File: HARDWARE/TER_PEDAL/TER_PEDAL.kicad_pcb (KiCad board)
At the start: 4 copper layers, 78.6 x 34.5 mm, 58 parts, among them J1 DEBUG, J2 APPS_1, J3 RJ45_Shielded, J4 APPS_2, J5 BPPS_1, J6 SteerSensor, SW1 RST, U1 STM32F103C8Tx, U2 TSR_1-2450, U3 LM1117MP-3.3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

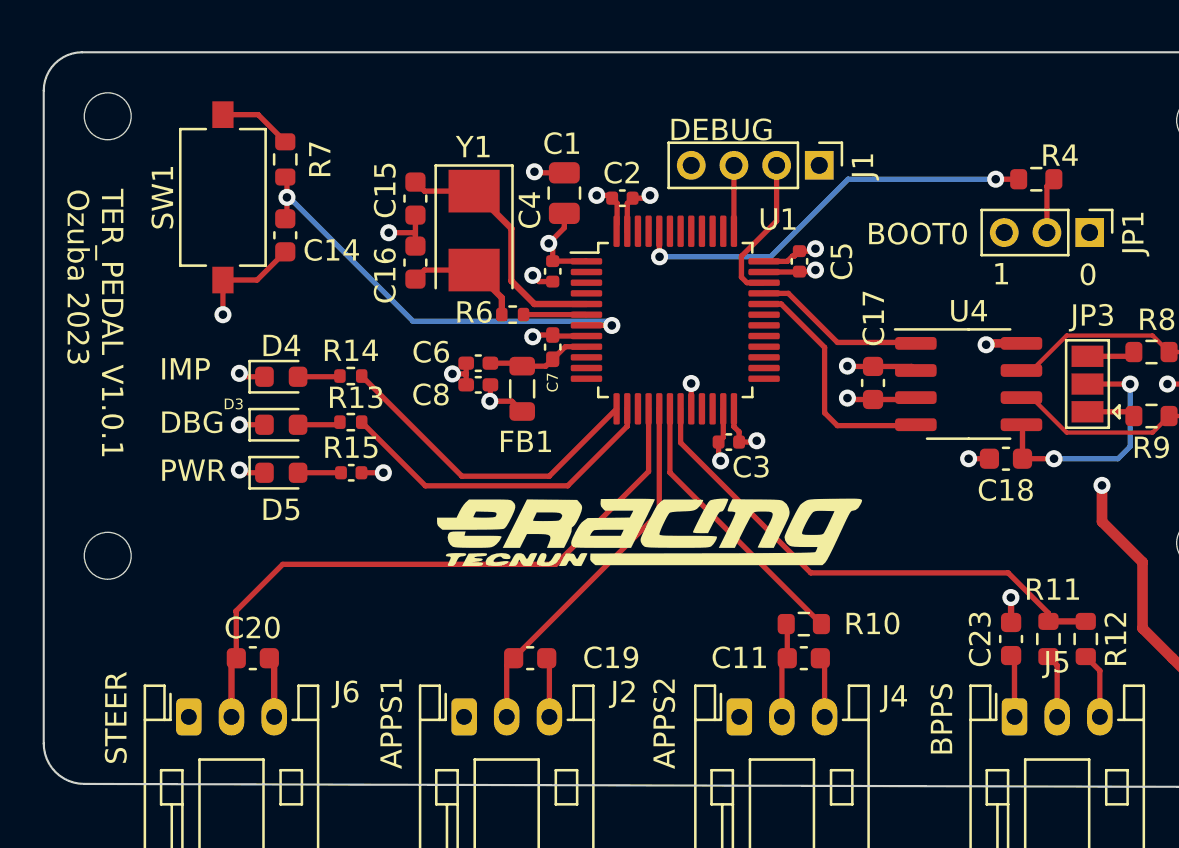
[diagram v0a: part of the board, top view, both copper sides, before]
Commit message: Added pull down resistors for adc to prevent floating value when disconnected signals, added LABELS lots of labels
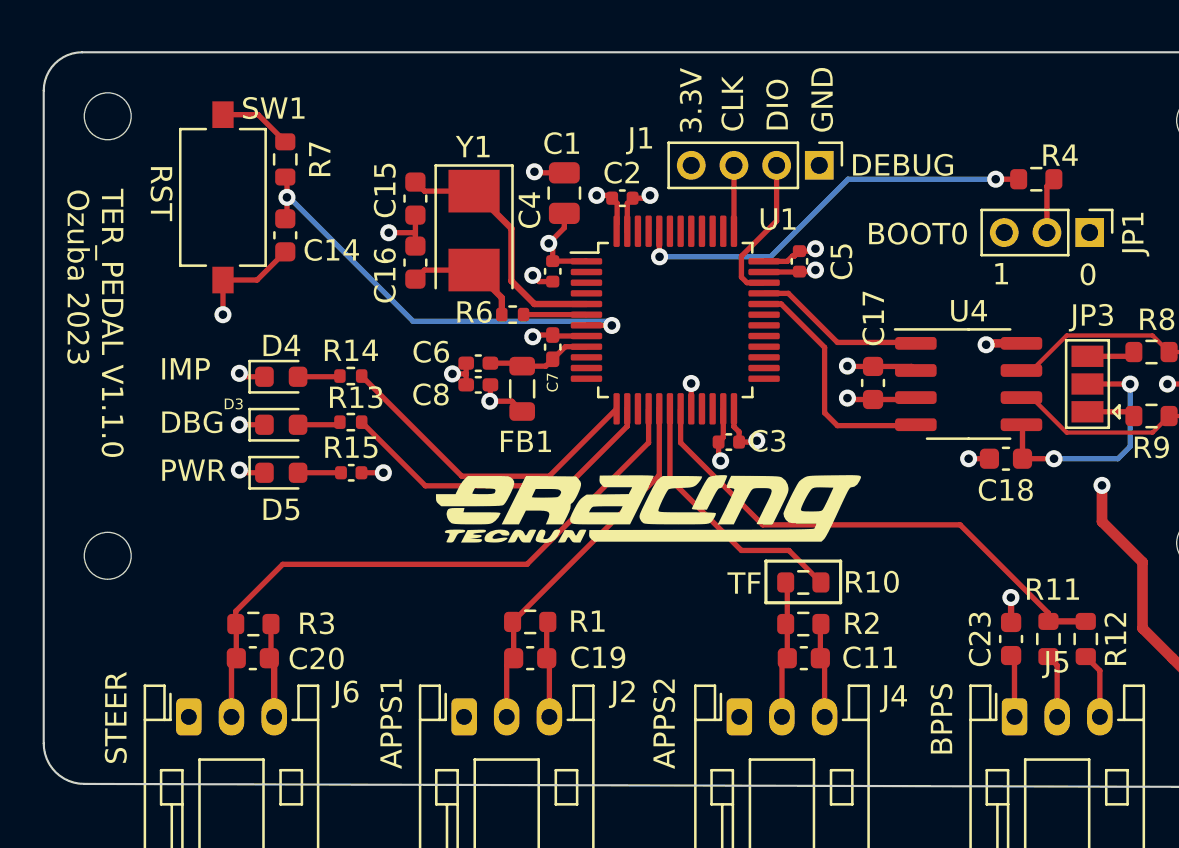
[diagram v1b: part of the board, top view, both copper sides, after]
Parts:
- added R1: 10k, Resistor_SMD:R_0603_1608Metric, F.Cu at (134.2, 102.9)
- added R2: 10k, Resistor_SMD:R_0603_1608Metric, F.Cu at (147.0, 103.0)
- added R3: 10k, Resistor_SMD:R_0603_1608Metric, F.Cu at (121.2, 103.0)
- moved R10 1.95 mm to (147.0, 101.0)
- moved G*** 1.10 mm to (139.8, 97.6)
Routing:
- net GND: track 57.0 -> 61.9 mm
- net /SENSORS/SENS_2: track 4.47 -> 6.43 mm
- net /MICRO/STEER_ADC: track 30.1 -> 29.3 mm
- net /MICRO/APPS_2_ADC: track 13.0 -> 12.4 mm
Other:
- board text added: "3.3V"
- board text added: "CLK"
- board text added: "DIO"
- board text added: "GND"
- board text added: "RST"
- board text added: "TER_PEDAL V1.1.0 Ozuba 2023"
- board text added: "TF"
- board text removed: "TER_PEDAL V1.0.1 Ozuba 2023"

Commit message: condensador señal brake
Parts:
- removed C23: 10u, Capacitor_SMD:C_0603_1608Metric
- added C21: 390u, Capacitor_SMD:C_0603_1608Metric, F.Cu at (157.1, 103.9)
- moved R11 0.43 mm to (158.9, 103.9)
- moved R12 0.43 mm to (160.6, 103.9)
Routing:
- net +5V: track 6.84 -> 3.90 mm

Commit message: Hecho layout
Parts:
- removed C17: 100n, Capacitor_SMD:C_0603_1608Metric
- removed C18: 4.7n, Capacitor_SMD:C_0603_1608Metric
- removed J1: DEBUG, Connector_PinHeader_2.00mm:PinHeader_1x04_P2.00mm_Vertical
- removed JP3: TermEnable, Jumper:SolderJumper-3_P1.3mm_Open_Pad1.0x1.5mm
- added C31: 100nF, Capacitor_SMD:C_0603_1608Metric, F.Cu at (148.4, 91.7)
- added C32: 4.7nF, Capacitor_SMD:C_0603_1608Metric, F.Cu at (154.6, 95.2)
- added FL2: ACT45B-510-2P-TL003, ACT45B-510-2P-TL003:FIL_ACT45B-510-2P-TL003, F.Cu at (165.0, 91.9)
- added J7: DEBUG, Connector_PinHeader_1.27mm:PinHeader_2x05_P1.27mm_Vertical, F.Cu at (147.4, 78.3)
- added JP2: SolderJumper_3_Open, Jumper:SolderJumper-3_P1.3mm_Open_Pad1.0x1.5mm, B.Cu at (167.9, 92.1)
- added R16: 100k, Resistor_SMD:R_0603_1608Metric, F.Cu at (149.6, 78.9)
- added R32: 50R, Resistor_SMD:R_0805_2012Metric, F.Cu at (169.6, 94.3)
- added R5: 100k, Resistor_SMD:R_0603_1608Metric, F.Cu at (140.2, 79.0)
- R8: value 50R -> 100k
- R9: footprint Resistor_SMD:R_0603_1608Metric -> Resistor_SMD:R_0805_2012Metric
- moved R8 21.5 mm to (143.4, 82.0)
- moved R9 7.31 mm to (169.7, 89.7), turned to 90 degrees
- moved D2 7.27 mm to (159.6, 91.8), turned to 180 degrees
- moved U4 1.90 mm to (152.9, 91.7)
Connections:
- D2 pad 1: /CAN/CAN+ -> Net-(U4-CANL)
- D2 pad 2: /CAN/CAN- -> Net-(U4-CANH)
- R8 pad 1: /CAN/CAN+ -> /MICRO/SWCLK
- R8 pad 2: Net-(JP3-B) -> GND
- R9 pad 1: Net-(JP3-A) -> /CAN/CAN+
- R9 pad 2: /CAN/CAN- -> Net-(JP2-A)
- U4 pad 6: /CAN/CAN- -> Net-(U4-CANL)
- U4 pad 7: /CAN/CAN+ -> Net-(U4-CANH)
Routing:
- net /MICRO/NRST: track 20.9 -> 34.1 mm
- net /CAN/CAN+: track 19.4 -> 8.38 mm
- net /CAN/CAN-: track 21.1 -> 10.2 mm
- net Net-(U4-CANL): track 0.00 -> 8.20 mm
- net Net-(U4-CANH): track 0.00 -> 8.02 mm
- net /MICRO/SWDIO: track 7.09 -> 12.0 mm
- net /MICRO/SWCLK: track 3.09 -> 7.98 mm
- net Net-(JP2-A): track 0.00 -> 4.46 mm, vias 0 -> 1
- net Net-(JP2-B): track 0.00 -> 4.00 mm, vias 0 -> 1
- net +3.3V: track 41.8 -> 45.8 mm, vias 8 -> 9
- net /CAN/VREF: track 12.1 -> 15.7 mm, vias 2 -> 1
- net Net-(JP3-B): track 2.26 -> 0.00 mm
- net Net-(JP3-A): track 2.26 -> 0.00 mm
- net /CAN/CAN_TX: track 8.08 -> 6.22 mm
- net GND: track 61.5 -> 62.8 mm
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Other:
- board text removed: "3.3V"
- board text removed: "CLK"
- board text removed: "DIO"
- board text removed: "GND"

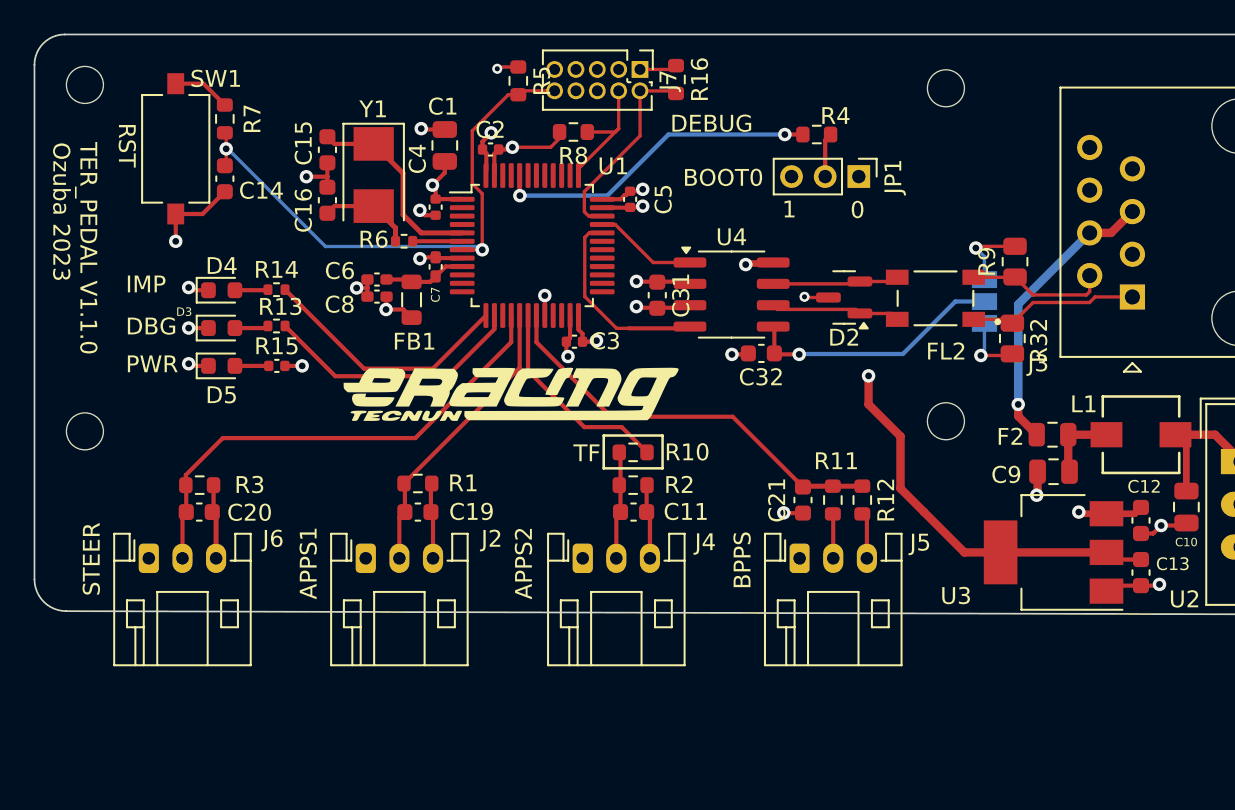
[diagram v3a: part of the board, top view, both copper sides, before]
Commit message: Added voltage followers to sensing, improved can circuitri, improved layout, waiting for routing
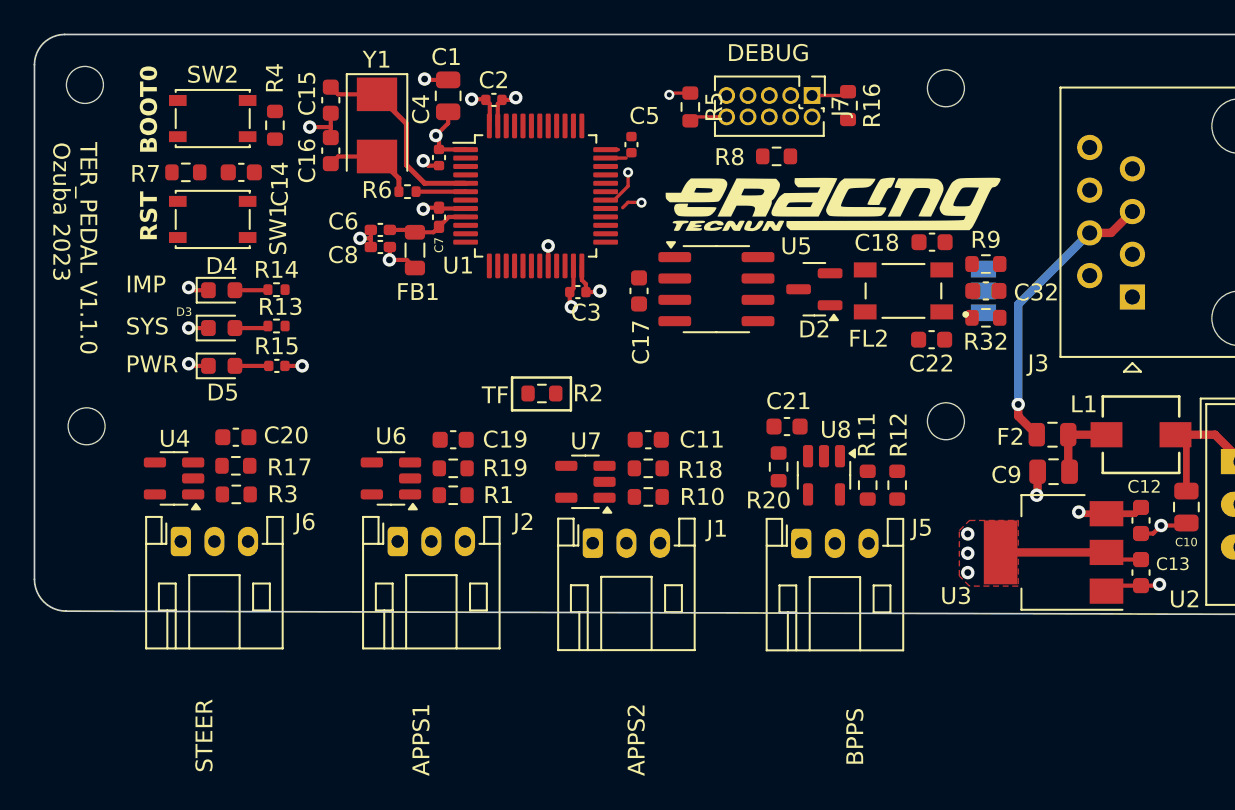
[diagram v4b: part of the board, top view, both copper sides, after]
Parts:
- removed C31: 100nF, Capacitor_SMD:C_0603_1608Metric
- removed J4: APPS_2, Connector_JST:JST_PH_S3B-PH-K_1x03_P2.00mm_Horizontal
- removed JP1: BOOT0, Connector_PinHeader_2.00mm:PinHeader_1x03_P2.00mm_Vertical
- added C17: 100n, Capacitor_SMD:C_0603_1608Metric, F.Cu at (147.3, 91.5)
- added C18: 10p, Capacitor_SMD:C_0603_1608Metric, F.Cu at (164.8, 88.5)
- added C22: 10p, Capacitor_SMD:C_0603_1608Metric, F.Cu at (164.8, 94.3)
- added J1: APPS_2, Connector_JST:JST_PH_S3B-PH-K_1x03_P2.00mm_Horizontal, F.Cu at (144.6, 106.5)
- added R17: 100, Resistor_SMD:R_0603_1608Metric, F.Cu at (123.4, 101.8)
- added R18: 100, Resistor_SMD:R_0603_1608Metric, F.Cu at (147.9, 102.0)
- added R19: 100, Resistor_SMD:R_0603_1608Metric, F.Cu at (136.3, 102.0)
- added R20: 100, Resistor_SMD:R_0603_1608Metric, F.Cu at (155.7, 101.9)
- added SW2: BOOT0, Button_Switch_SMD:SW_SPST_PTS810, F.Cu at (122.0, 81.2)
- added U5: TCAN332, Package_SO:SOIC-8_3.9x4.9mm_P1.27mm, F.Cu at (151.9, 91.3)
- added U6: LM321, Package_TO_SOT_SMD:SOT-23-5, F.Cu at (132.6, 102.6)
- added U7: LM321, Package_TO_SOT_SMD:SOT-23-5, F.Cu at (144.2, 102.8)
- added U8: LM321, Package_TO_SOT_SMD:SOT-23-5, F.Cu at (158.3, 102.4)
- C11, C19, C20: value 10u -> 160n
- C21: value 390u -> 160n
- D3: value LED -> SYS
- D4: value LED -> IMP
- D5: value LED -> PWR
- R1, R3: value 10k -> 100k
- R10: value 2k -> 100k
- R2: value 10k -> 0R
- R32, R9: value 50R -> 120R; footprint Resistor_SMD:R_0805_2012Metric -> Resistor_SMD:R_0603_1608Metric
- SW1: footprint Button_Switch_SMD:SW_Tactile_SPST_NO_Straight_CK_PTS636Sx25SMTRLFS -> Button_Switch_SMD:SW_SPST_PTS810
- U4: value SN65HVD230 -> LM321; footprint Package_SO:SOIC-8_3.9x4.9mm_P1.27mm -> Package_TO_SOT_SMD:SOT-23-5
- moved U4 34.9 mm to (119.7, 102.6), turned to 180 degrees
- moved R4 32.2 mm to (125.7, 81.6), turned to 90 degrees
- moved G*** 22.2 mm to (158.9, 86.3)
- moved C32 13.9 mm to (168.0, 91.5)
- moved R8 12.2 mm to (155.5, 83.5)
- moved R5 10.3 mm to (150.4, 80.5)
- moved R16 10.3 mm to (159.8, 80.4)
- moved J7 10.3 mm to (157.6, 79.8)
- moved R2 7.69 mm to (141.6, 97.5)
- moved C20 4.95 mm to (123.4, 100.2), turned to 180 degrees
- moved C19 4.79 mm to (136.3, 100.3), turned to 180 degrees
- moved SW1 4.74 mm to (122.0, 87.2), turned to 180 degrees
- moved C21 4.47 mm to (156.2, 99.5), turned to 0 degrees
- moved C11 4.39 mm to (147.9, 100.3), turned to 180 degrees
- moved R7 3.94 mm to (120.4, 84.4), turned to 0 degrees
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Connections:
- net /DBG_LED renamed /SYS
- C11 pad 1: /SENSORS/SENS_2 -> /MICRO/APPS_2_ADC
- C19 pad 1: /SENSORS/SENS_1 -> /MICRO/APPS_1_ADC
- C32 pad 1: /CAN/VREF -> Net-(JP2-C)
- D2 pad 1: Net-(U4-CANL) -> Net-(U5-CANL)
- D2 pad 2: Net-(U4-CANH) -> Net-(U5-CANH)
- FL2 pad 3: Net-(U4-CANH) -> Net-(U5-CANH)
- FL2 pad 4: Net-(U4-CANL) -> Net-(U5-CANL)
- J3 pad 3: unconnected-(J3-Pad3) -> +24V
- J3 pad 6: unconnected-(J3-Pad6) -> GND
- J6 pad 2: /MICRO/STEER_ADC -> Net-(J6-Pin_2)
- JP2 pad 2: /CAN/VREF -> Net-(JP2-C)
- R10 pad 1: /MICRO/APPS_2_ADC -> GND
- R11 pad 2: /MICRO/BPPS_ADC -> Net-(U8-+)
- R12 pad 1: /MICRO/BPPS_ADC -> Net-(U8-+)
- R2 pad 1: GND -> +3.3V
- R2 pad 2: /SENSORS/SENS_2 -> Net-(J1-Pin_1)
- R3 pad 2: /MICRO/STEER_ADC -> Net-(J6-Pin_2)
- R4 pad 1: Net-(JP1-C) -> /MICRO/BOOT0
- R4 pad 2: /MICRO/BOOT0 -> GND
- U1 pad 17: /SENSORS/SENS_1 -> /MICRO/APPS_1_ADC
- U4 pad 1: /CAN/CAN_TX -> Net-(J6-Pin_2)
- U4 pad 3: +3.3V -> Net-(U4--)
- U4 pad 4: /CAN/CAN_RX -> Net-(U4--)
- U4 pad 5: /CAN/VREF -> +3.3V
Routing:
- net GND: track 62.8 -> 29.5 mm, vias 21 -> 15
- net /MICRO/NRST: track 34.1 -> 2.26 mm, vias 2 -> 0
- net /MICRO/STEER_ADC: track 29.3 -> 0.00 mm
- net /MICRO/BPPS_ADC: track 24.6 -> 0.00 mm
- net +3.3V: track 45.8 -> 25.2 mm
- net /MICRO/BOOT0: track 19.5 -> 0.00 mm, vias 2 -> 0
- net /SENSORS/SENS_1: track 17.4 -> 0.00 mm
- net /CAN/VREF: track 15.7 -> 0.00 mm, vias 1 -> 0
- net /SYS: track 15.7 -> 0.00 mm
- net /IMP_LED: track 15.2 -> 0.00 mm
- net /MICRO/APPS_2_ADC: track 12.4 -> 0.00 mm
- net /MICRO/SWDIO: track 12.0 -> 0.00 mm
- net /CAN/CAN_RX: track 11.9 -> 0.00 mm
- net /CAN/CAN-: track 10.2 -> 0.00 mm
- net /CAN/CAN+: track 8.38 -> 0.00 mm
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- added copper zone on F.Cu, net +3.3V
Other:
- board text added: "SYS"
- board text removed: "0"
- board text removed: "1"
- board text removed: "DBG"

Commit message: çMejorado layout
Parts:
- removed J6: SteerSensor, Connector_JST:JST_PH_S3B-PH-K_1x03_P2.00mm_Horizontal
- added J4: APPS_1, Connector_JST:JST_PH_S3B-PH-K_1x03_P2.00mm_Horizontal, F.Cu at (73.0, 115.2)
- added R21: 4.7k, Resistor_SMD:R_0603_1608Metric, F.Cu at (110.5, 142.0)
- added R22: 4.7k, Resistor_SMD:R_0603_1608Metric, F.Cu at (145.8, 140.8)
- added R23: 100, Resistor_SMD:R_0603_1608Metric, F.Cu at (81.9, 119.2)
- R1, R10: value 100k -> 9.1k
- R17: value 100 -> 9.1k
- R3: value 100k -> 4.7k
- moved R12 99.3 mm to (70.9, 140.9), turned to 0 degrees
- moved U8 99.2 mm to (67.2, 141.6), turned to 180 degrees
- moved R11 98.3 mm to (70.9, 142.6), turned to 180 degrees
- moved J5 97.5 mm to (67.6, 145.4)
- moved C21 93.4 mm to (70.9, 137.7), turned to 180 degrees
- moved R20 92.6 mm to (70.9, 139.3), turned to 0 degrees
- moved R3 47.1 mm to (76.9, 111.1)
- moved U4 47.1 mm to (73.2, 110.2)
- moved R17 47.1 mm to (76.9, 109.4)
- moved C20 47.1 mm to (76.9, 107.7)
- moved J2 46.3 mm to (107.2, 144.8)
- moved U6 46.3 mm to (106.8, 141.1)
- moved C19 45.0 mm to (110.5, 137.2)
- moved R1 44.9 mm to (110.5, 140.4)
- moved R19 44.9 mm to (110.5, 138.8)
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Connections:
- J2 pad 1: +3.3V -> +5V
- R1 pad 2: /SENSORS/SENS_1 -> Net-(U6-+)
- R10 pad 2: /SENSORS/SENS_2 -> Net-(U7-+)
- R17 pad 1: Net-(U4--) -> GND
- R17 pad 2: /MICRO/STEER_ADC -> Net-(U4-+)
- R2 pad 1: +3.3V -> +5V
- R3 pad 1: GND -> Net-(U4-+)
- R3 pad 2: Net-(J6-Pin_2) -> Net-(J4-Pin_2)
- U4 pad 1: Net-(J6-Pin_2) -> Net-(U4-+)
- U6 pad 1: /SENSORS/SENS_1 -> Net-(U6-+)
- U7 pad 1: /SENSORS/SENS_2 -> Net-(U7-+)
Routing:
- net +5V: track 3.90 -> 5.47 mm, vias 1 -> 2
- net +3.3V: vias 9 -> 10

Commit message: avanzando
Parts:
- moved R20 96.6 mm to (159.1, 99.7)
- moved R11 96.6 mm to (159.1, 102.9), turned to 0 degrees
- moved U8 96.6 mm to (155.3, 101.9)
- moved C21 96.6 mm to (159.1, 98.1)
- moved R12 96.6 mm to (159.1, 101.3)
- moved J5 96.6 mm to (155.8, 105.9)
- moved C20 46.7 mm to (122.5, 98.1)
- moved J4 46.6 mm to (118.6, 105.9)
- moved U4 46.4 mm to (118.9, 101.9)
- moved R17 46.4 mm to (122.6, 101.2), turned to 180 degrees
- moved R3 46.4 mm to (122.6, 102.9)
- moved R21 45.8 mm to (134.2, 102.9), turned to 180 degrees
- moved R19 45.8 mm to (134.2, 99.6)
- moved U6 45.8 mm to (130.5, 101.9)
- moved C19 45.8 mm to (134.2, 98.0)
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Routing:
- net /MICRO/BOOT0: track 0.00 -> 23.3 mm, vias 0 -> 2
- net /MICRO/NRST: track 2.26 -> 21.8 mm, vias 0 -> 2
- net /MICRO/SWDIO: track 0.00 -> 17.4 mm
- net /MICRO/SWCLK: track 0.00 -> 15.5 mm
- net +5V: track 5.47 -> 18.7 mm
- net GND: track 29.5 -> 39.1 mm, vias 15 -> 20
- net +3.3V: track 25.2 -> 31.3 mm, vias 10 -> 13
- net Net-(SW1-B): track 0.00 -> 6.02 mm
- net Net-(U6-+): track 0.00 -> 4.89 mm
- net Net-(U6--): track 0.00 -> 4.55 mm
- net /SENSORS/SENS_1: track 0.00 -> 3.17 mm
- net unconnected-(U1-PA9-Pad30): track 1.92 -> 0.00 mm, vias 1 -> 0
- net +24V: track 17.3 -> 19.1 mm

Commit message: avanzando layout
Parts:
- moved H2 0.24 mm to (114.3, 99.3)
- moved C5 0.06 mm to (147.1, 83.3)
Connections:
- net Net-(U5-CANH) renamed /CAN/can+
- net Net-(U5-CANL) renamed /CAN/can-
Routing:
- net GND: track 39.1 -> 63.9 mm, vias 20 -> 36
- net /MICRO/BPPS_ADC: track 0.00 -> 24.3 mm
- net /MICRO/STEER_ADC: track 0.00 -> 22.1 mm
- net /SYS: track 0.00 -> 14.6 mm
- net /CAN/CAN_RX: track 0.00 -> 14.0 mm
- net /MICRO/NRST: track 21.8 -> 35.6 mm, vias 2 -> 3
- net /CAN/CAN-: track 0.00 -> 13.7 mm
- net /MICRO/APPS_2_ADC: track 0.00 -> 13.7 mm
- net /IMP_LED: track 0.00 -> 12.7 mm
- net /MICRO/APPS_1_ADC: track 0.00 -> 12.0 mm
- net /CAN/CAN+: track 0.00 -> 11.0 mm
- net +3.3V: track 31.3 -> 39.6 mm, vias 13 -> 17
- net /CAN/CAN_TX: track 0.00 -> 7.04 mm
- net /CAN/can-: track 0.00 -> 6.67 mm
- net /CAN/can+: track 0.00 -> 6.59 mm
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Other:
- board text added: "una pista de 0,5 mm aguanta 2 amps vamos sobradisimos"

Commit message: avanzando layout
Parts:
- moved R9 2.19 mm to (170.1, 90.4)
- moved C17 2.19 mm to (149.5, 92.0)
- moved C32 2.19 mm to (170.1, 92.0)
- moved FL2 2.19 mm to (165.2, 91.9)
- moved R32 2.19 mm to (170.1, 93.6)
- moved U5 2.19 mm to (154.1, 91.8)
- moved C22 2.19 mm to (166.9, 94.9)
- moved D2 2.19 mm to (159.9, 91.9)
- moved C18 2.19 mm to (166.9, 89.1)
- moved G*** 2.19 mm to (161.0, 86.8)
- moved JP2 2.19 mm to (170.0, 92.0)
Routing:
- net Net-(JP2-C): track 3.74 -> 0.92 mm
- net Net-(JP2-B): track 3.16 -> 1.09 mm
- net Net-(JP2-A): track 3.02 -> 1.09 mm
- net /CAN/CAN-: track 13.7 -> 12.0 mm
- net /CAN/CAN_TX: track 7.04 -> 8.48 mm
- net +24V: track 19.1 -> 20.5 mm
- net /CAN/CAN+: track 11.0 -> 10.3 mm
- net GND: track 63.9 -> 63.2 mm
